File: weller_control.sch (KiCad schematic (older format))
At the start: 20 parts, among them J2 AudioJack3_Ground_SwitchR, Q1 DMP2018LFK, U2 LTC4440IS6, U3 MCP603-xCH

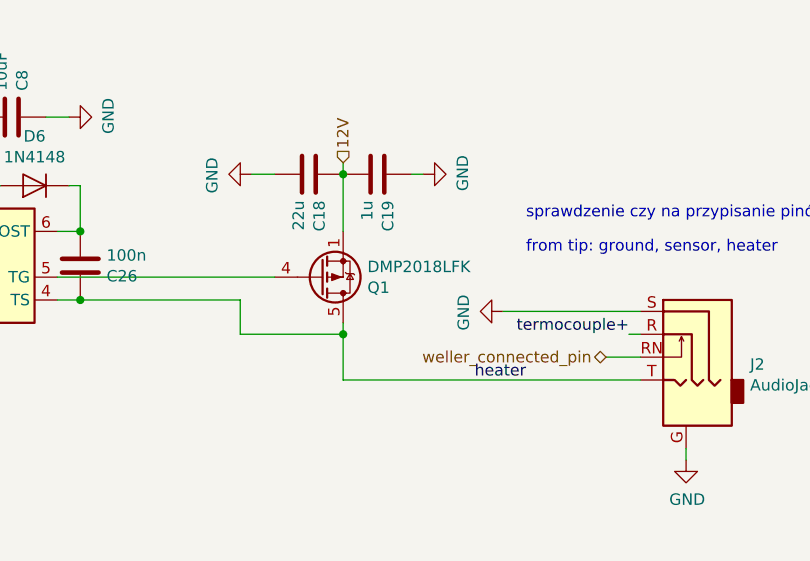
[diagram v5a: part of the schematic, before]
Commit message: zmiana tranzystora
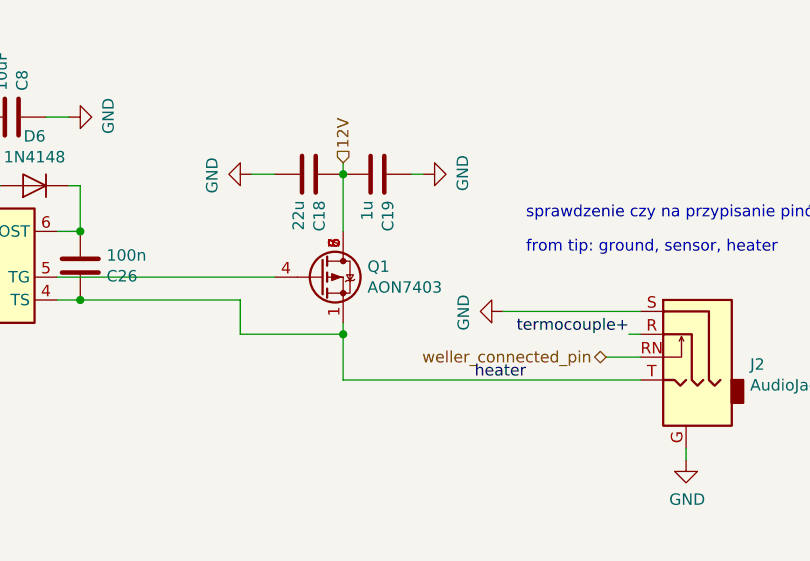
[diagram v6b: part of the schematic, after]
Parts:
- removed Q1: DMP2018LFK, Package_SON:Diodes_PowerDI3333-8, symbol Transistor_FET:DMP3013SFV
- added Q1: AON7403, symbols:DFN_3X3_EP, symbol russian-nixies:AON7403
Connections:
- net 12V: now also Q1.5 (D), Q1.6 (D), Q1.7 (D), Q1.8 (D)
- net heater: now also Q1.1 (S), Q1.2 (S), Q1.3 (S)
- net at U2.5 (TG): now also Q1.4 (G)
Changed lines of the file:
@@
 from tip: ground, sensor, heater
-$Comp
-L Transistor_FET:DMP3013SFV Q1
-U 1 1 5CBB49B6
-P 6200 3050
-F 0 "Q1" H 6406 3096 50  0000 L CNN
-F 1 "DMP2018LFK" H 6406 3005 50  0000 L CNN
-F 2 "Package_SON:Diodes_PowerDI3333-8" H 6400 2975 50  0001 L CIN
-F 3 "https://www.diodes.com/assets/Datasheets/DMP3013SFV.pdf" V 6200 3050 50  0001 L CNN
-F 4 "${KISYS3DMOD}/Package_DFN_QFN.3dshapes/DFN-8-1EP_3x3mm_P0.65mm_EP1.55x2.4mm.wrl" H 6200 3050 50  0001 C CNN "Pole4"
-	1    6200 3050
-	1    0    0    1
-$EndComp
 $Comp
 L power:GND #PWR?
@@
 Wire Wire Line
 	7000 3200 7600 3200
+$Comp
+L russian-nixies:AON7403 Q1
+U 1 1 5D1F5BBF
+P 6200 3050
+F 0 "Q1" H 6406 3096 50  0000 L CNN
+F 1 "AON7403" H 6406 3005 50  0000 L CNN
+F 2 "symbols:DFN_3X3_EP" H 6400 2975 50  0001 L CIN
+F 3 "https://www.diodes.com/assets/Datasheets/DMP3013SFV.pdf" V 6200 3050 50  0001 L CNN
+	1    6200 3050
+	1    0    0    -1
+$EndComp
 $EndSCHEMATC

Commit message: update front endu do termopary i przełącznika zasilającego
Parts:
- removed R10: 100k, Resistor_SMD:R_0603_1608Metric, symbol Device:R
- removed R9: 1meg, Resistor_SMD:R_0603_1608Metric, symbol Device:R
- removed U3: MCP603-xCH, TO_SOT_Packages_SMD:SOT-23-6, symbol Amplifier_Operational:MCP603-xCH
- added C33: 10n, Capacitor_SMD:C_0603_1608Metric_Pad1.05x0.95mm_HandSolder, symbol Device:C
- added C34, C35: 100n, Capacitor_SMD:C_0603_1608Metric_Pad1.05x0.95mm_HandSolder, symbol Device:C
- added R18, R25: 10meg, Resistor_SMD:R_0603_1608Metric, symbol Device:R
- added R19: 1meg, Resistor_SMD:R_0603_1608Metric, symbol Device:R
- added R26: 100k, Resistor_SMD:R_0603_1608Metric, symbol Device:R
- added R27: 150, Resistor_SMD:R_0603_1608Metric, symbol Device:R
- added R28: 68, Resistor_SMD:R_0603_1608Metric, symbol Device:R
- added U3: MCP6N16, Package_SO:MSOP-8_3x3mm_P0.65mm, symbol russian-nixies:MCP6N16
- C11: value n.c. -> 100n
- C6: value 100n -> 10n
- R11: value 270 -> 1k
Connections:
- net 3.3V_analog: now also R18.1, R19.2, U3.8 (VDD)
- net GND: now also R11.1, C33.1; no longer R11.2
- net GNDA: now also R25.2, R28.1, U3.4 (VSS)
- net termocouple_out: now also C11.1
- net at R12.2: now also C35.1, R26.2, U3.7 (VOUT); no longer C11.1
- net at C6.1, R8.2: now also C34.1, R18.2, U3.3 (V+)
- new net: R19.1, U3.1 (EN)
- new net: C33.2, C34.2, R11.2, U3.2 (V-)
- new net: R25.1, U3.5 (VREF)
- new net: C35.2, R26.1, R27.2, U3.6 (VFG)
- new net: R27.1, R28.2
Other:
- note added: "moze MCP96L00 ?"
- note added: "możliwie bliskie połaczenie do pinu z Jack\n"
- moved on the sheet: C10, C11, C18, C19, C26, C6, C7, C8, C9, D6, J2, Q1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
